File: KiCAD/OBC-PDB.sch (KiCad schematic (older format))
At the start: 0 parts

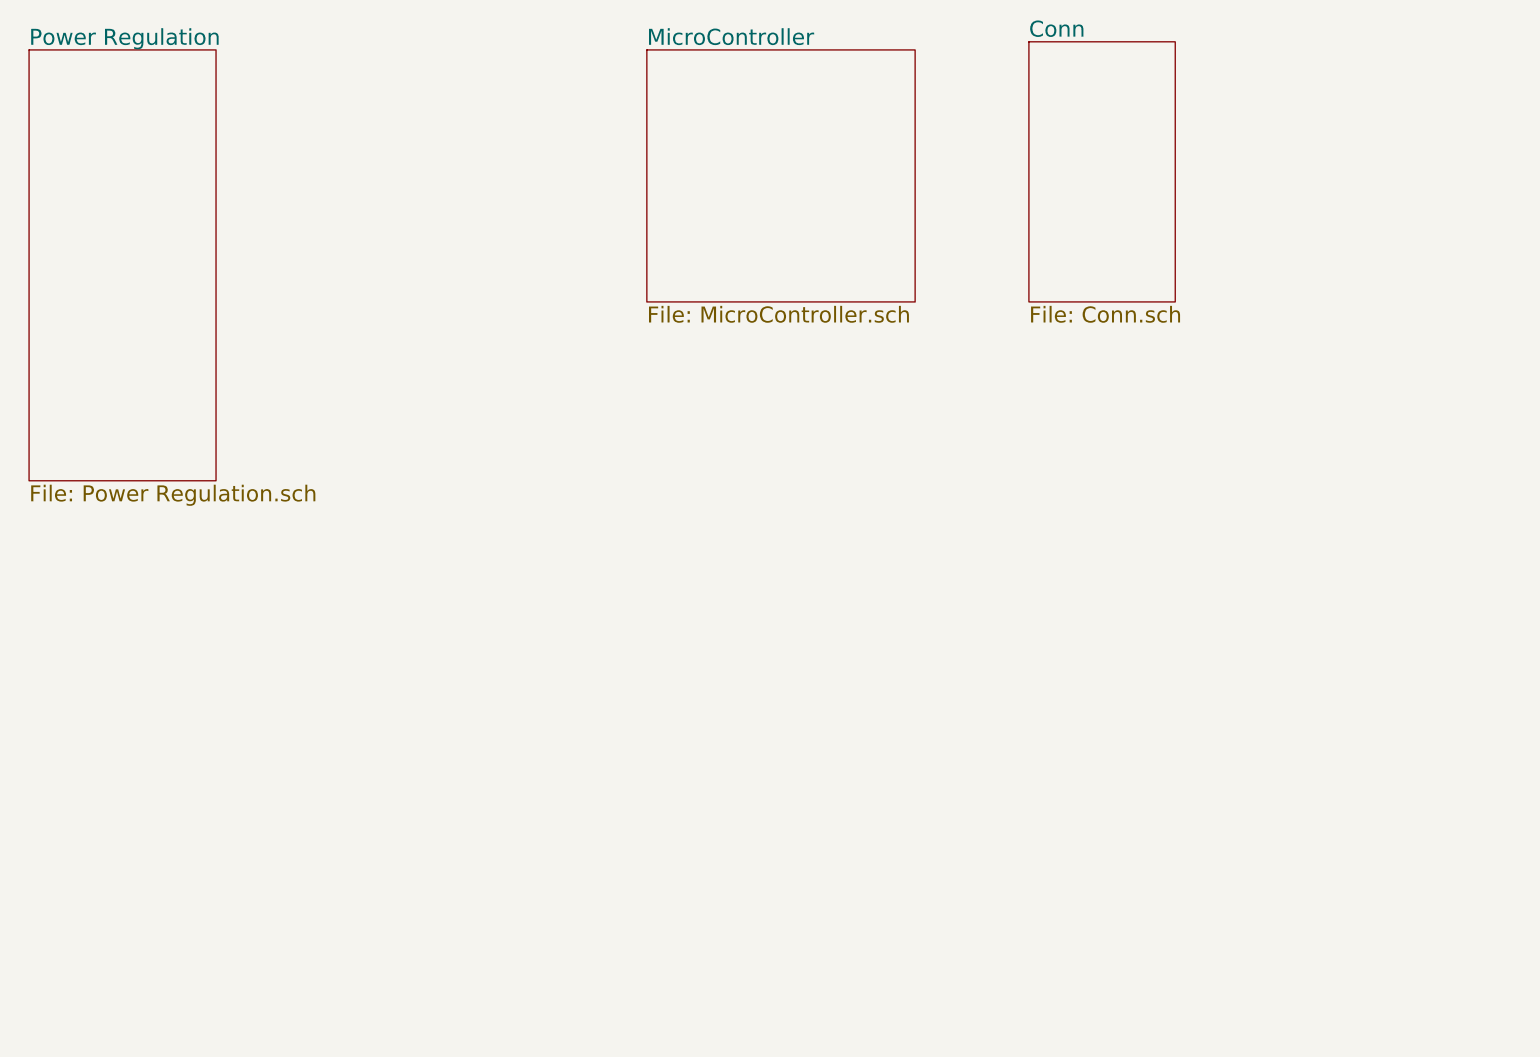
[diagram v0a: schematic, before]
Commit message: completed 5V buck schematic and setup
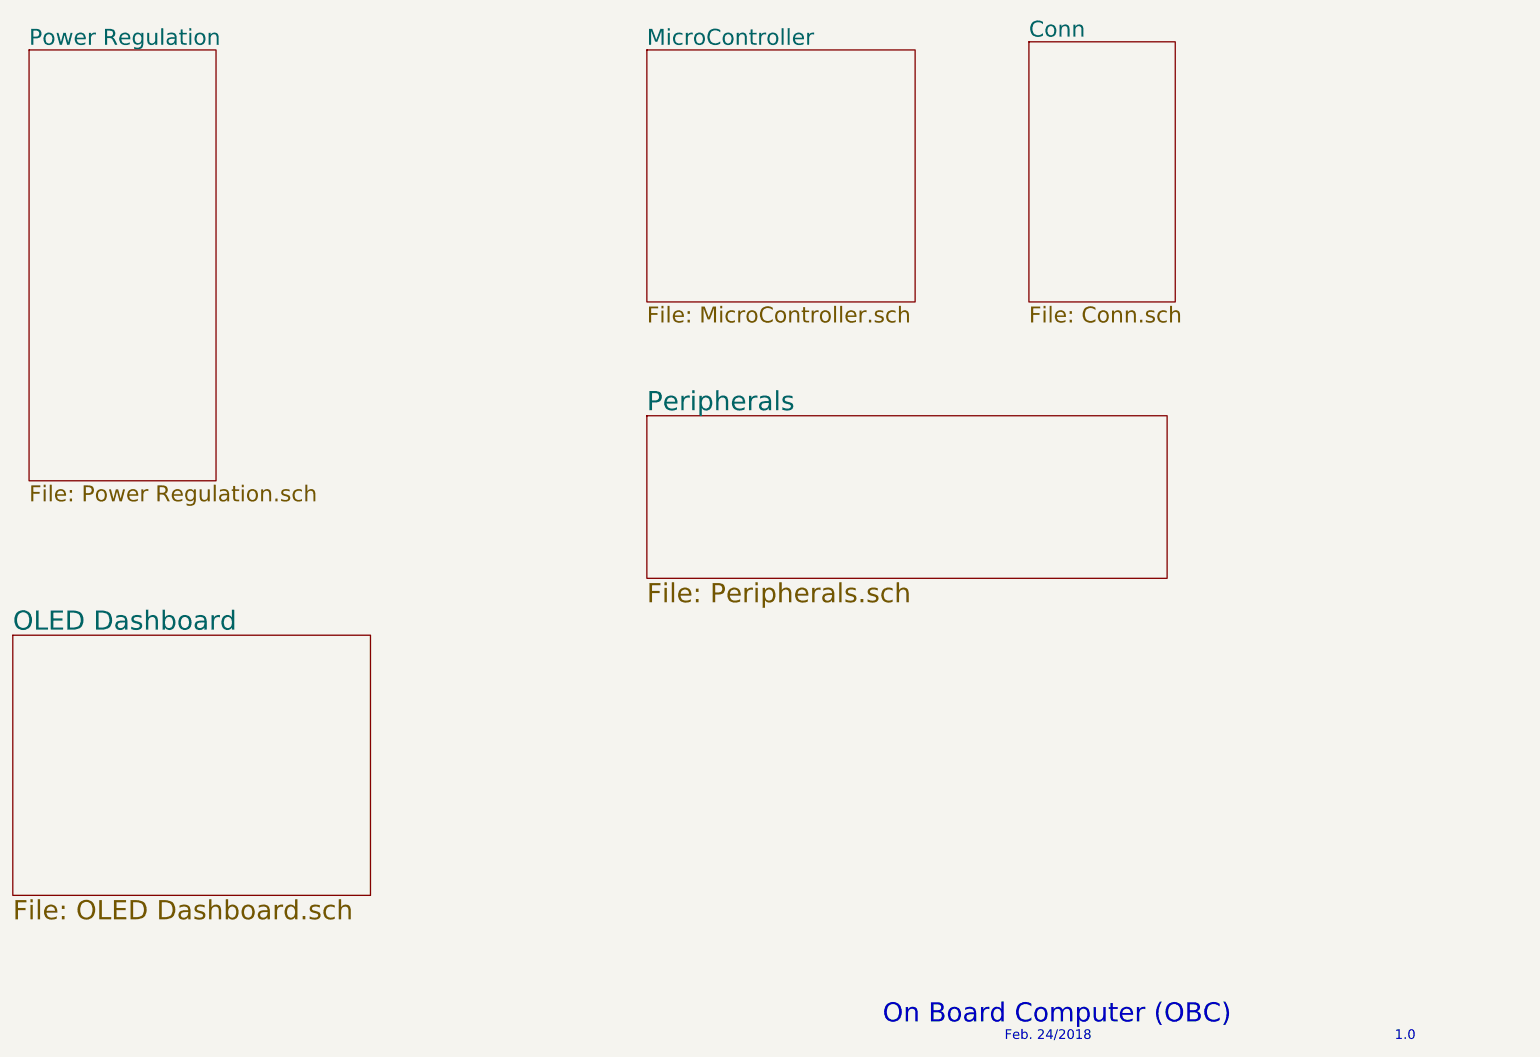
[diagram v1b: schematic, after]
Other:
- note added: "1.0"
- note added: "Feb. 24/2018"
- note added: "On Board Computer (OBC)"

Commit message: Schematic small fix
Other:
- note added: "Electronic Instrument Cluster (EIC)"
- note removed: "On Board Computer (OBC)"
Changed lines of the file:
@@
 LIBS:valves
 LIBS:TPS565208
-LIBS:Switch
+LIBS:isolators
+LIBS:74xgxx
+LIBS:ac-dc
+LIBS:actel
+LIBS:allegro
+LIBS:Altera
+LIBS:analog_devices
+LIBS:battery_management
+LIBS:bbd
+LIBS:bosch
+LIBS:brooktre
+LIBS:cmos_ieee
+LIBS:dc-dc
+LIBS:diode
+LIBS:elec-unifil
+LIBS:ESD_Protection
+LIBS:ftdi
+LIBS:gennum
+LIBS:graphic_symbols
+LIBS:hc11
+LIBS:infineon
+LIBS:intersil
+LIBS:ir
+LIBS:Lattice
+LIBS:leds
+LIBS:LEM
+LIBS:logic_programmable
+LIBS:maxim
+LIBS:mechanical
+LIBS:microchip_dspic33dsc
+LIBS:microchip_pic10mcu
+LIBS:microchip_pic12mcu
+LIBS:microchip_pic16mcu
+LIBS:microchip_pic18mcu
+LIBS:microchip_pic24mcu
+LIBS:microchip_pic32mcu
+LIBS:modules
+LIBS:motor_drivers
+LIBS:motors
+LIBS:msp430
+LIBS:nordicsemi
+LIBS:nxp
+LIBS:nxp_armmcu
+LIBS:onsemi
+LIBS:Oscillators
+LIBS:Power_Management
+LIBS:powerint
+LIBS:pspice
+LIBS:references
+LIBS:relays
+LIBS:rfcom
+LIBS:RFSolutions
+LIBS:sensors
+LIBS:silabs
+LIBS:stm8
+LIBS:stm32
+LIBS:supertex
+LIBS:switches
+LIBS:transf
+LIBS:triac_thyristor
+LIBS:ttl_ieee
+LIBS:video
+LIBS:wiznet
+LIBS:Worldsemi
+LIBS:Xicor
+LIBS:zetex
+LIBS:Zilog
+LIBS:DRV8825
+LIBS:MAX6675
 LIBS:OBC-PDB-cache
 EELAYER 25 0
@@
 Feb. 24/2018
 Text Notes 7400 7550 0    118  ~ 0
-On Board Computer (OBC)
+Electronic Instrument Cluster (EIC)
 Text Notes 10550 7650 0    59   ~ 0
 1.0
